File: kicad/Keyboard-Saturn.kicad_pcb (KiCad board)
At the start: 2 copper layers, 438.9 x 124.3 mm, 215 parts, among them J1 OLED_128x32, SW0 SW_Push, SW1 SW_Push, SW10 SW_Push, SW100 SW_Push, SW101 SW_Push, SW102 SW_Push, SW103 SW_Push, SW104 SW_Push, SW11 SW_Push, SW12 SW_Push, SW13 SW_Push, SW14 SW_Push, SW15 SW_Push, SW16 SW_Push, SW17 SW_Push, SW18 SW_Push, SW19 SW_Push, SW2 SW_Push, SW20 SW_Push, SW21 SW_Push, SW22 SW_Push, SW23 SW_Push, SW24 SW_Push, SW25 SW_Push, SW26 SW_Push, SW27 SW_Push, SW28 SW_Push, SW29 SW_Push, SW30 SW_Push, SW31 SW_Push, SW32 SW_Push, SW33 SW_Push, SW34 SW_Push, SW35 SW_Push, SW36 SW_Push, SW37 SW_Push, SW38 SW_Push, SW39 SW_Push, SW4 SW_Push, SW40 SW_Push, SW41 SW_Push, SW42 SW_Push, SW43 SW_Push, SW44 SW_Push, SW45 SW_Push, SW46 SW_Push, SW47 SW_Push, SW48 SW_Push, SW49 SW_Push, SW5 SW_Push, SW50 SW_Push, SW51 SW_Push, SW52 SW_Push, SW53 SW_Push, SW54 SW_Push, SW55 SW_Push, SW56 SW_Push, SW57 SW_Push, SW58 SW_Push, SW59 SW_Push, SW6 SW_Push, SW60 SW_Push, SW61 SW_Push, SW62 SW_Push, SW63 SW_Push, SW64 SW_Push, SW65 SW_Push, SW66 SW_Push, SW67 SW_Push, SW68 SW_Push, SW69 SW_Push, SW7 SW_Push, SW70 SW_Push, SW71 SW_Push, SW72 SW_Push, SW73 SW_Push, SW74 SW_Push, SW75 SW_Push, SW76 SW_Push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

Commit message: added SN34HC165N to kicad
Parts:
- removed R1, R2: 2k, Resistor_THT:R_Axial_DIN0204_L3.6mm_D1.6mm_P7.62mm_Horizontal
- removed U2: MCP23017_SO, Package_SO:SOIC-28W_7.5x17.9mm_P1.27mm
- added U3: SN74HC165N, Keyboard-Saturn:DIP794W45P254L1969H508Q16, F.Cu at (383.0, 59.3)
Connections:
- U1 pad 1: unconnected-(U1-GPIO0-Pad1)_1 -> Net-(U1-GPIO0)
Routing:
- net Net-(U1-GPIO0): track 0.00 -> 77.0 mm
- net row 5: track 539.0 -> 557.5 mm
- net Net-(U1-GPIO26_ADC0): track 58.6 -> 73.2 mm, vias 1 -> 0
- net row 6: track 441.6 -> 427.7 mm
- net GND: track 267.8 -> 280.3 mm, vias 1 -> 0
- net row 2: track 470.9 -> 480.9 mm
- net +3.3V: track 172.8 -> 165.4 mm, vias 3 -> 4
- net row 1: track 471.5 -> 476.7 mm
- net row 3: track 457.7 -> 460.2 mm, vias 0 -> 1
- net row 4: track 564.5 -> 566.2 mm
- net Net-(U1-GPIO27_ADC1): track 53.7 -> 54.0 mm, vias 1 -> 2

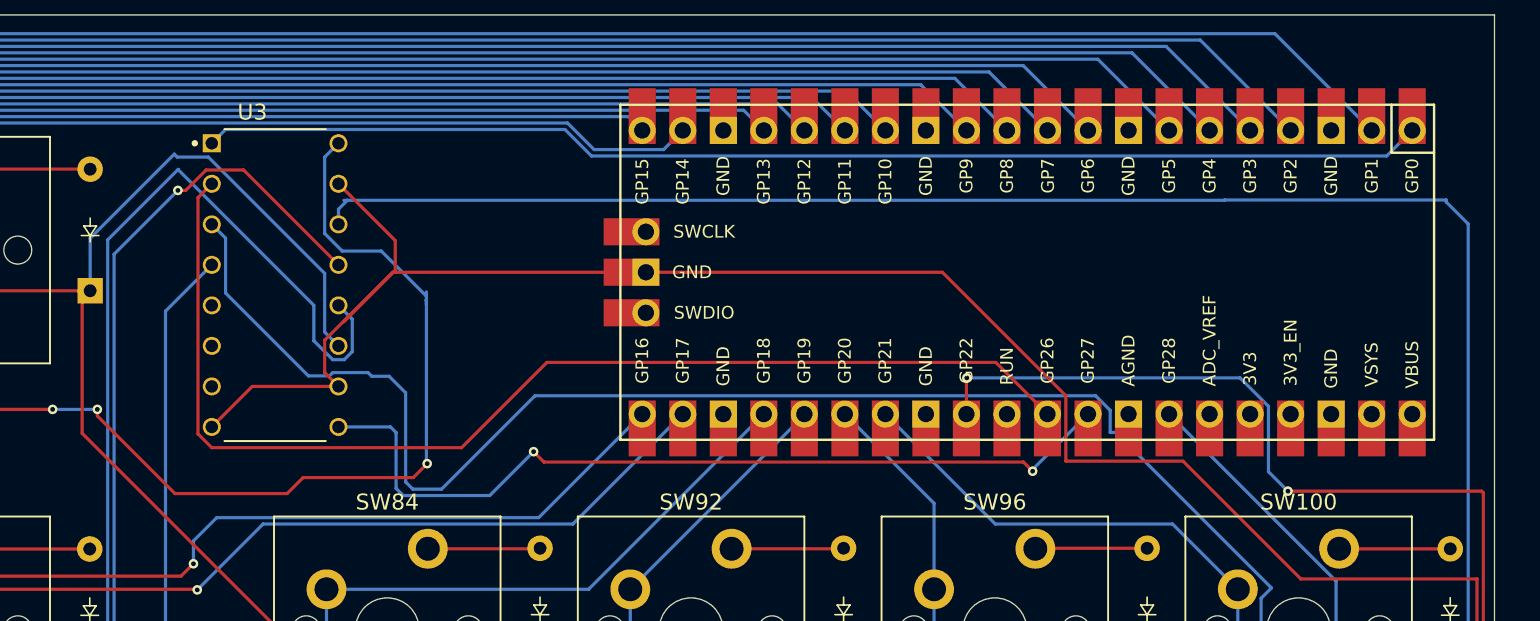
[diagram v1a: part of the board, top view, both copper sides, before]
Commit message: generate gerber, update PCB step + finshed PCB wiring
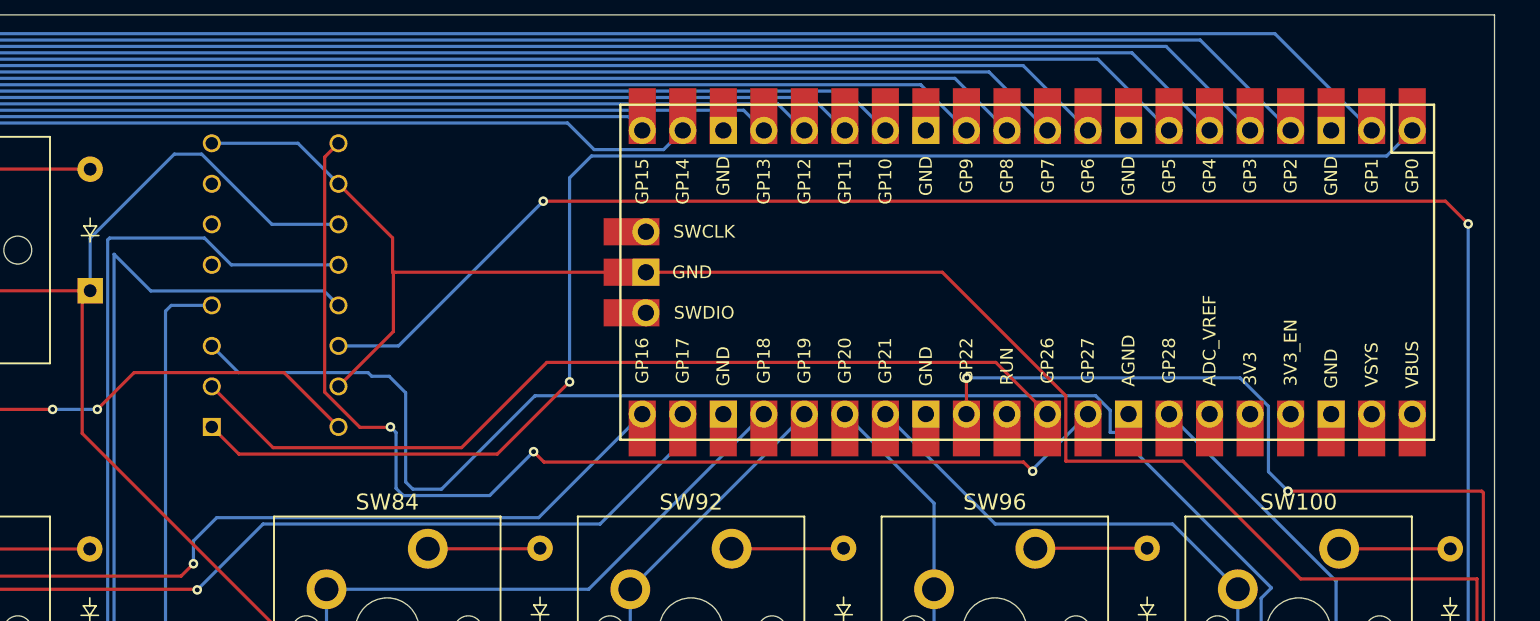
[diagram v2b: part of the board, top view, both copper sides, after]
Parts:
- U3: moved to B.Cu
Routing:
- net +3.3V: track 165.4 -> 133.9 mm, vias 4 -> 3
- net Net-(U1-GPIO27_ADC1): track 54.0 -> 71.7 mm, vias 2 -> 3
- net Net-(U1-GPIO26_ADC0): track 73.2 -> 57.5 mm
- net Net-(U1-GPIO0): track 77.0 -> 91.8 mm, vias 0 -> 1
- net row 2: track 480.9 -> 469.2 mm
- net row 5: track 557.5 -> 552.1 mm
- net row 1: track 476.7 -> 471.3 mm
- net GND: track 280.3 -> 275.1 mm
- net row 3: track 460.2 -> 456.8 mm, vias 1 -> 0
- net row 4: track 566.2 -> 568.5 mm, vias 0 -> 2
- net row 6: track 427.7 -> 426.7 mm
- net col 17: track 155.1 -> 156.1 mm

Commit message: update 3d model, and added copper fills
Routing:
- added copper zone on B.Cu, net GND
- added copper zone on F.Cu, net GND
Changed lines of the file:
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@@
 			(drillshape 0)
 			(scaleselection 1)
-			(outputdirectory "")
+			(outputdirectory "gbr/")
 		)
 	)
@@
 		(at 382.97 59.31)
 		(property "Reference" "U3"
-			(at -1.425 10.835 360)
+			(at -1.425 10.835 0)
 			(layer "B.SilkS")
 			(effects
@@
 		)
 		(property "Value" "SN74HC165N"
-			(at 0.605 -11.115 360)
+			(at 0.605 -11.115 0)
 			(layer "B.Fab")
 			(effects
@@
 		)
 		(property "Footprint" "Keyboard-Saturn:DIP794W45P254L1969H508Q16"
-			(at 0 0 360)
+			(at 0 0 0)
 			(layer "B.Fab")
 			(hide yes)
@@
 		)
 		(property "Datasheet" ""
-			(at 0 0 360)
+			(at 0 0 0)
 			(layer "B.Fab")
 			(hide yes)
@@
 		)
 		(property "Description" ""
-			(at 0 0 360)
+			(at 0 0 0)
 			(layer "B.Fab")
 			(hide yes)
@@
 		(net 172)
 	)
+	(zone
+		(net 114)
+		(net_name "GND")
+		(layers "F&B.Cu")
+		(hatch edge 0.5)
+		(connect_pads
+			(clearance 0.5)
+		)
+		(min_thickness 0.25)
+		(filled_areas_thickness no)
+		(fill yes
+			(thermal_gap 0.5)
+			(thermal_bridge_width 0.5)
+		)
+		(polygon
+			(pts
+				(xy 19.025 35.275) (xy 462.2 37.6) (xy 463.65 176.15) (xy 14.7 172.65) (xy 19.125 35.225) (xy 19.175 35.325)
+				(xy 20.2 35.325) (xy 20.875 35.4)
+			)
+		)
+	)
 )

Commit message: 90% done firmware, updated kicad files to match code
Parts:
- renumbered F2 to SW3, SW0 to SW80
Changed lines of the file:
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@@
 		(descr "MX keyswitch PCB Mount Keycap 1.00u")
 		(tags "MX Keyboard Keyswitch Switch PCB Cutout Keycap 1.00u")
-		(property "Reference" "SW0"
+		(property "Reference" "SW80"
 			(at 0 -8 0)
 			(layer "F.SilkS")
@@
 		(descr "MX keyswitch PCB Mount Keycap 1.00u")
 		(tags "MX Keyboard Keyswitch Switch PCB Cutout Keycap 1.00u")
-		(property "Reference" "F2"
+		(property "Reference" "SW3"
 			(at 0 -8 0)
 			(layer "F.SilkS")
